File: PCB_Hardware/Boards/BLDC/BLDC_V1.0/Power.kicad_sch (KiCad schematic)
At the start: 37 parts, among them J3 Conn_01x02_Pin, J4 Conn_01x02_Pin, Q2 IPT015N10N5, U11 AMS1117-3.3, U4 LMR38020, U5 LM5069MM-2, U6 TLV70233_SOT23-5

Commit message: Add DBcan transport refactor, BLDC V1.0 schematic + sim work, HAL submodule
- DBcan: replace bare-register driver with vendor-agnostic transport abstraction (core/, transports/, refactored bootloader driver, README)
- Add stm32g4xx_hal_driver as Firmware/libs submodule
- Add HAL config for BLDC board (stm32g4xx_hal_conf.h)
- BLDC V1.0: schematic edits across 10 sheets (footprint assignments, repositioning); design-doc README (gate-driver constraints, FET selection / TPH3R70APL, thermal analysis)
- ngspice simulation workflow (cap sweeps, half-bridge slow turn-on)
- Ignore .obsidian/ vault state and large simulation CSV exports
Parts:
- C10, C5, C8, C9: footprint (none) -> Capacitor_SMD:C_0805_2012Metric
- C11, C13, C29, C6, C7: footprint (none) -> Capacitor_SMD:C_0402_1005Metric
- C12, C14: footprint (none) -> Capacitor_SMD:C_0603_1608Metric
- D12, D13: footprint (none) -> LED_SMD:LED_0603_1608Metric
- D4: footprint (none) -> Diode_SMD:D_SMC
- J3, J4: footprint (none) -> Connector_AMASS:AMASS_XT30PW-M_1x02_P2.50mm_Horizontal
- R10, R7, R8, R9: footprint (none) -> Resistor_SMD:R_0805_2012Metric
- R11, R3, R4, R5: footprint (none) -> Resistor_SMD:R_0402_1005Metric
- R17, R21: footprint (none) -> Resistor_SMD:R_0603_1608Metric
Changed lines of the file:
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@@
 			)
 		)
-		(property "Footprint" ""
+		(property "Footprint" "Connector_AMASS:AMASS_XT30PW-M_1x02_P2.50mm_Horizontal"
 			(at 92.71 104.14 0)
 			(hide yes)
@@
 			)
 		)
-		(property "Footprint" ""
+		(property "Footprint" "Diode_SMD:D_SMC"
 			(at 111.76 109.22 0)
 			(hide yes)
@@
 			)
 		)
-		(property "Footprint" ""
+		(property "Footprint" "Capacitor_SMD:C_0402_1005Metric"
 			(at 192.7352 143.51 0)
 			(hide yes)
@@
 			)
 		)
-		(property "Footprint" ""
+		(property "Footprint" "Resistor_SMD:R_0402_1005Metric"
 			(at 220.472 116.84 90)
 			(hide yes)
@@
 			)
 		)
-		(property "Footprint" ""
+		(property "Footprint" "Capacitor_SMD:C_0805_2012Metric"
 			(at 301.9552 116.84 0)
 			(hide yes)
@@
 			)
 		)
-		(property "Footprint" ""
+		(property "Footprint" "Resistor_SMD:R_0402_1005Metric"
 			(at 276.352 123.19 90)
 			(hide yes)
@@
 			)
 		)
-		(property "Footprint" ""
+		(property "Footprint" "Capacitor_SMD:C_0402_1005Metric"
 			(at 220.6752 96.52 0)
 			(hide yes)
@@
 			)
 		)
-		(property "Footprint" ""
+		(property "Footprint" "Resistor_SMD:R_0805_2012Metric"
 			(at 146.812 140.97 90)
 			(hide yes)
@@
 			)
 		)
-		(property "Footprint" ""
+		(property "Footprint" "Capacitor_SMD:C_0603_1608Metric"
 			(at 127.9652 113.03 0)
 			(hide yes)
@@
 			)
 		)
-		(property "Footprint" ""
+		(property "Footprint" "Capacitor_SMD:C_0603_1608Metric"
 			(at 270.2052 204.47 0)
 			(hide yes)
@@
 			)
 		)
-		(property "Footprint" ""
+		(property "Footprint" "Resistor_SMD:R_0805_2012Metric"
 			(at 136.652 121.92 90)
 			(hide yes)
@@
 			)
 		)
-		(property "Footprint" ""
+		(property "Footprint" "Capacitor_SMD:C_0805_2012Metric"
 			(at 313.3852 116.84 0)
 			(hide yes)
@@
 			)
 		)
-		(property "Footprint" ""
+		(property "Footprint" "Capacitor_SMD:C_0402_1005Metric"
 			(at 234.6452 204.47 0)
 			(hide yes)
@@
 			)
 		)
-		(property "Footprint" ""
+		(property "Footprint" "Resistor_SMD:R_0603_1608Metric"
 			(at 210.058 92.71 90)
 			(hide yes)
@@
 			)
 		)
-		(property "Footprint" ""
+		(property "Footprint" "Resistor_SMD:R_0402_1005Metric"
 			(at 276.352 113.03 90)
 			(hide yes)
@@
 			)
 		)
-		(property "Footprint" ""
+		(property "Footprint" "Connector_AMASS:AMASS_XT30PW-M_1x02_P2.50mm_Horizontal"
 			(at 92.71 114.3 0)
 			(hide yes)
@@
 			)
 		)
-		(property "Footprint" ""
+		(property "Footprint" "LED_SMD:LED_0603_1608Metric"
 			(at 275.59 195.58 0)
 			(hide yes)
@@
 			)
 		)
-		(property "Footprint" ""
+		(property "Footprint" "LED_SMD:LED_0603_1608Metric"
 			(at 187.96 195.58 0)
 			(hide yes)
@@
 			)
 		)
-		(property "Footprint" ""
+		(property "Footprint" "Resistor_SMD:R_0402_1005Metric"
 			(at 201.422 139.7 90)
 			(hide yes)
@@
 			)
 		)
-		(property "Footprint" ""
+		(property "Footprint" "Resistor_SMD:R_0805_2012Metric"
 			(at 146.812 121.92 90)
 			(hide yes)
@@
 			)
 		)
-		(property "Footprint" ""
+		(property "Footprint" "Capacitor_SMD:C_0805_2012Metric"
 			(at 290.5252 116.84 0)
 			(hide yes)
@@
 			)
 		)
-		(property "Footprint" ""
+		(property "Footprint" "Resistor_SMD:R_0603_1608Metric"
 			(at 203.2 89.408 90)
 			(hide yes)
@@
 			)
 		)
-		(property "Footprint" ""
+		(property "Footprint" "Capacitor_SMD:C_0402_1005Metric"
 			(at 265.43 101.9048 0)
 			(hide yes)
@@
 			)
 		)
-		(property "Footprint" ""
+		(property "Footprint" "Resistor_SMD:R_0805_2012Metric"
 			(at 136.652 140.97 90)
 			(hide yes)
@@
 			)
 		)
-		(property "Footprint" ""
+		(property "Footprint" "Capacitor_SMD:C_0805_2012Metric"
 			(at 197.8152 113.03 0)
 			(hide yes)
@@
 			)
 		)
-		(property "Footprint" ""
+		(property "Footprint" "Capacitor_SMD:C_0402_1005Metric"
 			(at 210.5152 113.03 0)
 			(hide yes)

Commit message: migrated claude skills to opencode, and added to the schematic review skill. Also updated the readme with calculations for the BLDC driver and changed the sense resistors to 1m Ohm
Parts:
- C11: value 22n -> 33n
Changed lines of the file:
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@@
 			)
 		)
-		(property "Value" "22n"
+		(property "Value" "33n"
 			(at 195.58 140.9699 0)
 			(show_name no)

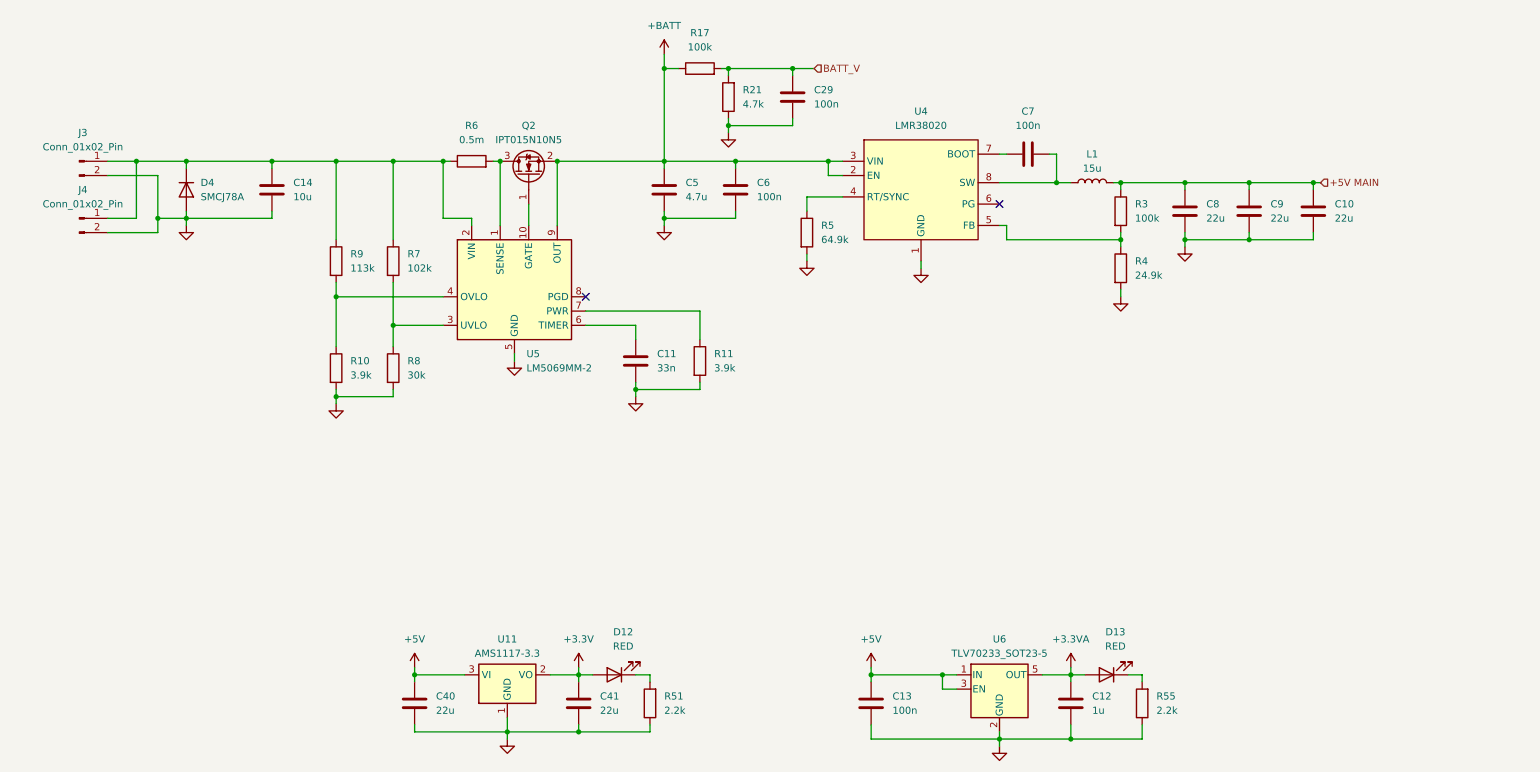
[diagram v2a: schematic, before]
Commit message: Created organization around the symbol lib and did a first pass layout of the BDLC
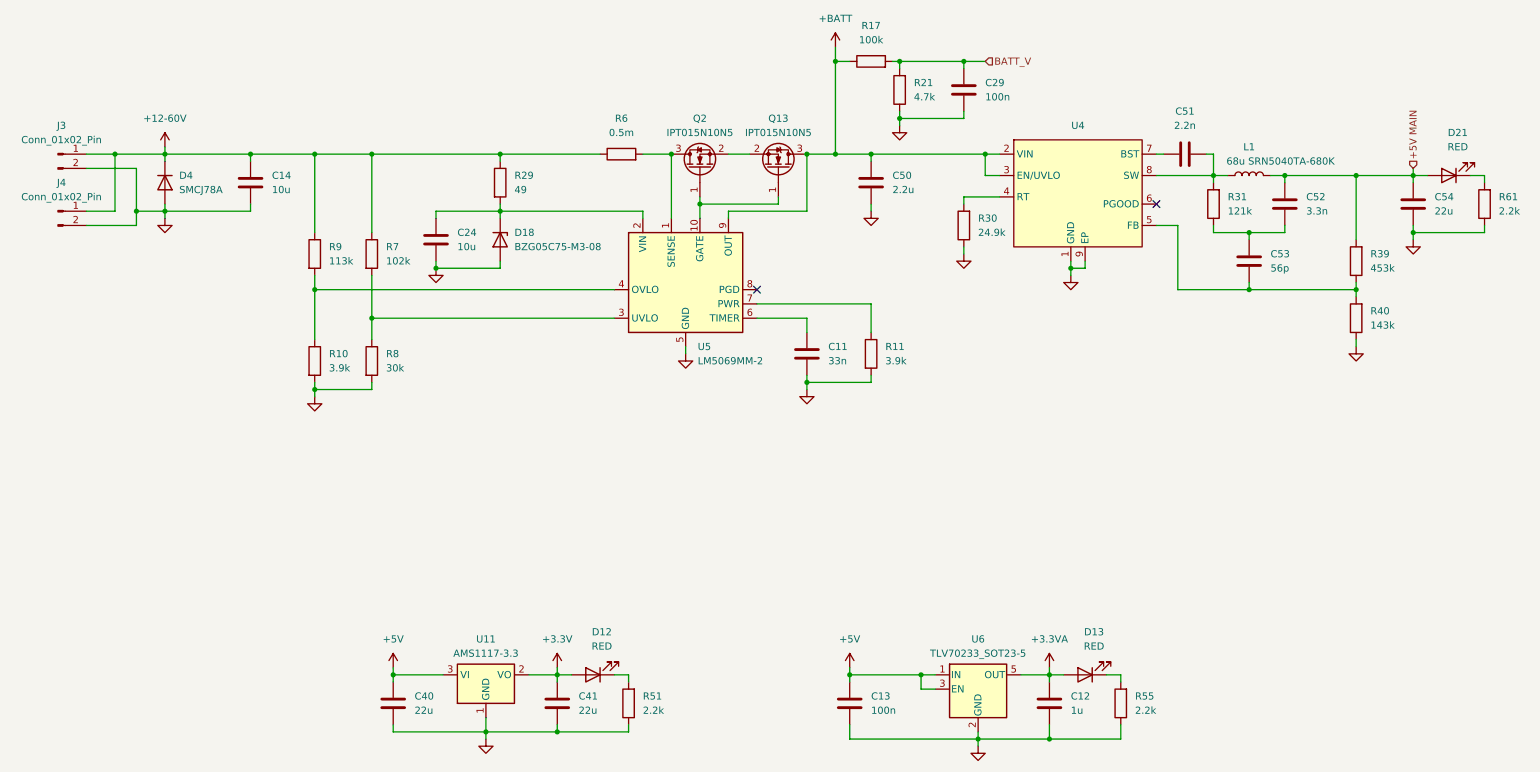
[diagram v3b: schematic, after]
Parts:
- removed C10, C8, C9: 22u, Capacitor_SMD:C_0805_2012Metric, symbol Device:C
- removed C5: 4.7u, Capacitor_SMD:C_0805_2012Metric, symbol Device:C
- removed C6, C7: 100n, Capacitor_SMD:C_0402_1005Metric, symbol Device:C
- removed R3: 100k, Resistor_SMD:R_0402_1005Metric, symbol Device:R
- removed R4: 24.9k, Resistor_SMD:R_0402_1005Metric, symbol Device:R
- removed R5: 64.9k, Resistor_SMD:R_0402_1005Metric, symbol Device:R
- removed U4: LMR38020, Package_SO:SO-8_3.9x4.9mm_P1.27mm, symbol DBRobot:LMR38020
- added C24: 10u, Capacitor_SMD:C_0603_1608Metric, symbol Device:C
- added C50: 2.2u, Capacitor_SMD:C_0805_2012Metric, symbol Device:C
- added C51: 2.2n, Capacitor_SMD:C_0402_1005Metric, symbol Device:C
- added C52: 3.3n, Capacitor_SMD:C_0402_1005Metric, symbol Device:C
- added C53: 56p, Capacitor_SMD:C_0402_1005Metric, symbol Device:C
- added C54: 22u, Capacitor_SMD:C_0805_2012Metric, symbol Device:C
- added D18: BZG05C75-M3-08, Diode_SMD:D_SMA, symbol Device:D_Zener
- added D21: RED, LED_SMD:LED_0603_1608Metric, symbol Device:LED
- added Q13: IPT015N10N5, Package_TO_SOT_SMD:Infineon_PG-HSOF-8-1, symbol Transistor_FET:IPT015N10N5
- added R29: 49, Resistor_SMD:R_0805_2012Metric, symbol Device:R
- added R30: 24.9k, Resistor_SMD:R_0402_1005Metric, symbol Device:R
- added R31: 121k, Resistor_SMD:R_0402_1005Metric, symbol Device:R
- added R39: 453k, Resistor_SMD:R_0402_1005Metric, symbol Device:R
- added R40: 143k, Resistor_SMD:R_0402_1005Metric, symbol Device:R
- added R61: 2.2k, Resistor_SMD:R_0402_1005Metric, symbol Device:R
- added U4: (no value), Package_SO:SOIC-8-1EP_3.9x4.9mm_P1.27mm_EP2.29x3mm, symbol DBRobot_Buck_Converter:LM516x
- L1: value 15u -> 68u SRN5040TA-680K
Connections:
- net +5V MAIN: now also C52.2, C54.1, D21.2 (A), R39.2
- net +BATT: now also C50.1, Q13.3 (D), U4.2 (VIN), U4.3 (EN/UVLO); no longer Q2.2 (S)
- net GND: now also C24.2, C50.2, C54.2, D18.2 (A), R30.1, R40.1, R61.1, U4.1 (GND), U4.9 (EP)
- net +12-60V: now reaches C14.1, D4.1 (K), J3.1 (Pin_1), J4.1 (Pin_1), R6.1, R7.1, R9.1
- net +12-60V: now also R29.1; no longer U5.2 (VIN)
- net at L1.1: now also C51.2, R31.2, U4.8 (SW)
- net at Q2.1 (G), U5.10 (GATE): now also Q13.1 (G)
- new net: C52.1, C53.2, R31.1
- new net: D21.1 (K), R61.2
- new net: C53.1, R39.1, R40.2, U4.5 (FB)
- new net: Q13.2 (S), Q2.2 (S)
- new net: C24.1, D18.1 (K), R29.2, U5.2 (VIN)
- new net: C51.1, U4.7 (BST)
- new net: R30.2, U4.4 (RT)
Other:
- moved on the sheet: C11, C12, C13, C14, C29, C40, C41, D12, D13, D4, J3, J4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

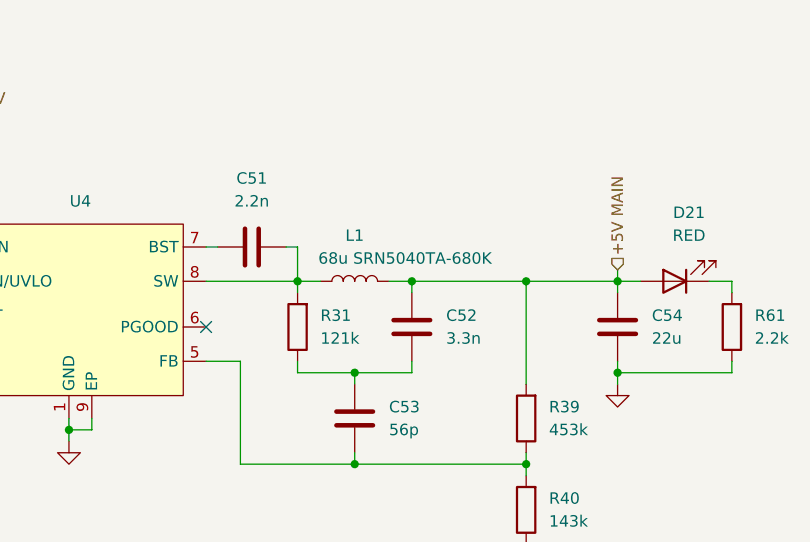
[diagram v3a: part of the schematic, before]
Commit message: complete redo of the BLDC layout
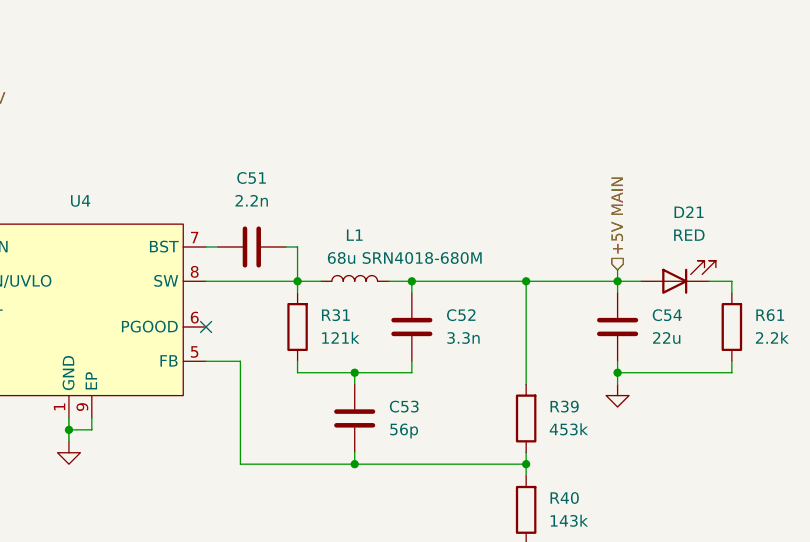
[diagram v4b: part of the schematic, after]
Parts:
- L1: value 68u SRN5040TA-680K -> 68u SRN4018-680M; footprint (none) -> Inductor_SMD:L_Bourns-SRN4018
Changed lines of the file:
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@@
 			)
 		)
-		(property "Value" "68u SRN5040TA-680K"
+		(property "Value" "68u SRN4018-680M"
 			(at 306.578 104.14 90)
 			(show_name no)
@@
 			)
 		)
-		(property "Footprint" ""
+		(property "Footprint" "Inductor_SMD:L_Bourns-SRN4018"
 			(at 300.99 106.68 0)
 			(hide yes)
